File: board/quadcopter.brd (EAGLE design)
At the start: 100 x 80 mm, 41 parts, among them IC1 LD1117V33

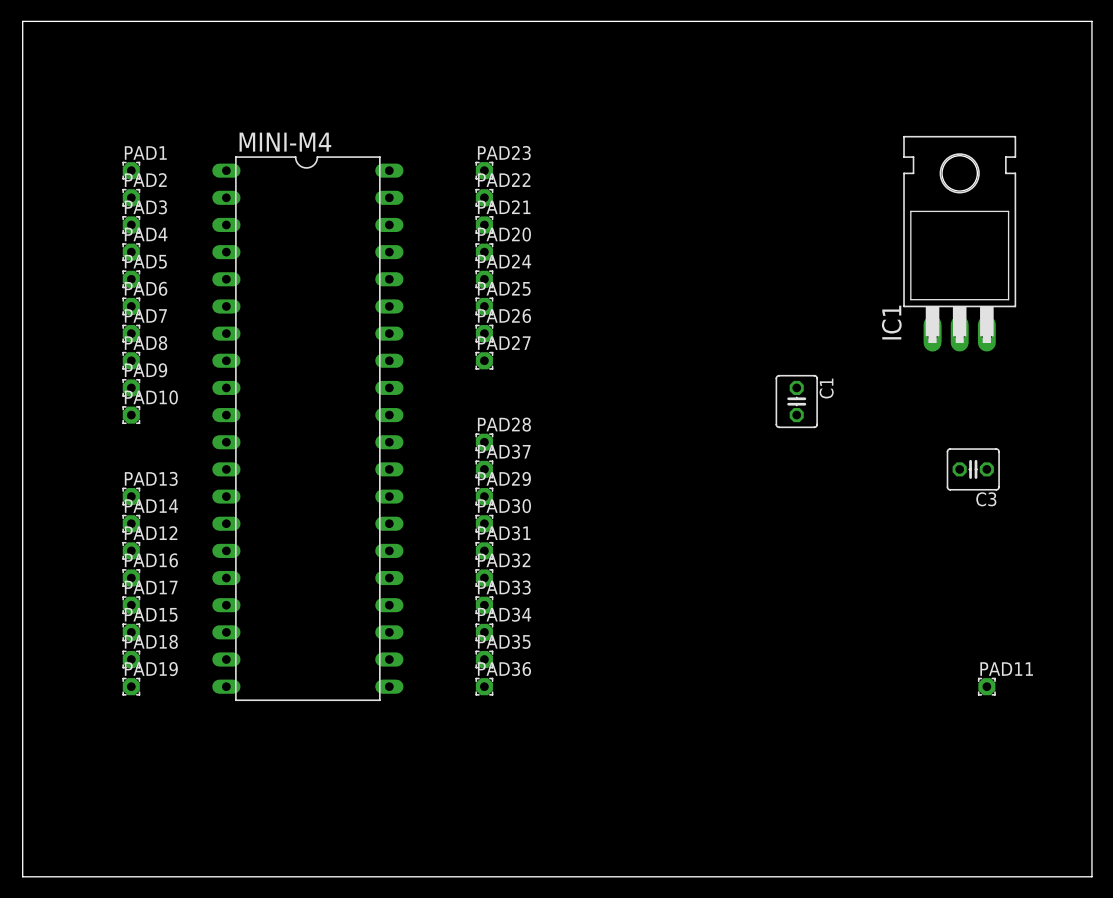
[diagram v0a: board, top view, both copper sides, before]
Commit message: updated the board layout and routed the voltage regulator
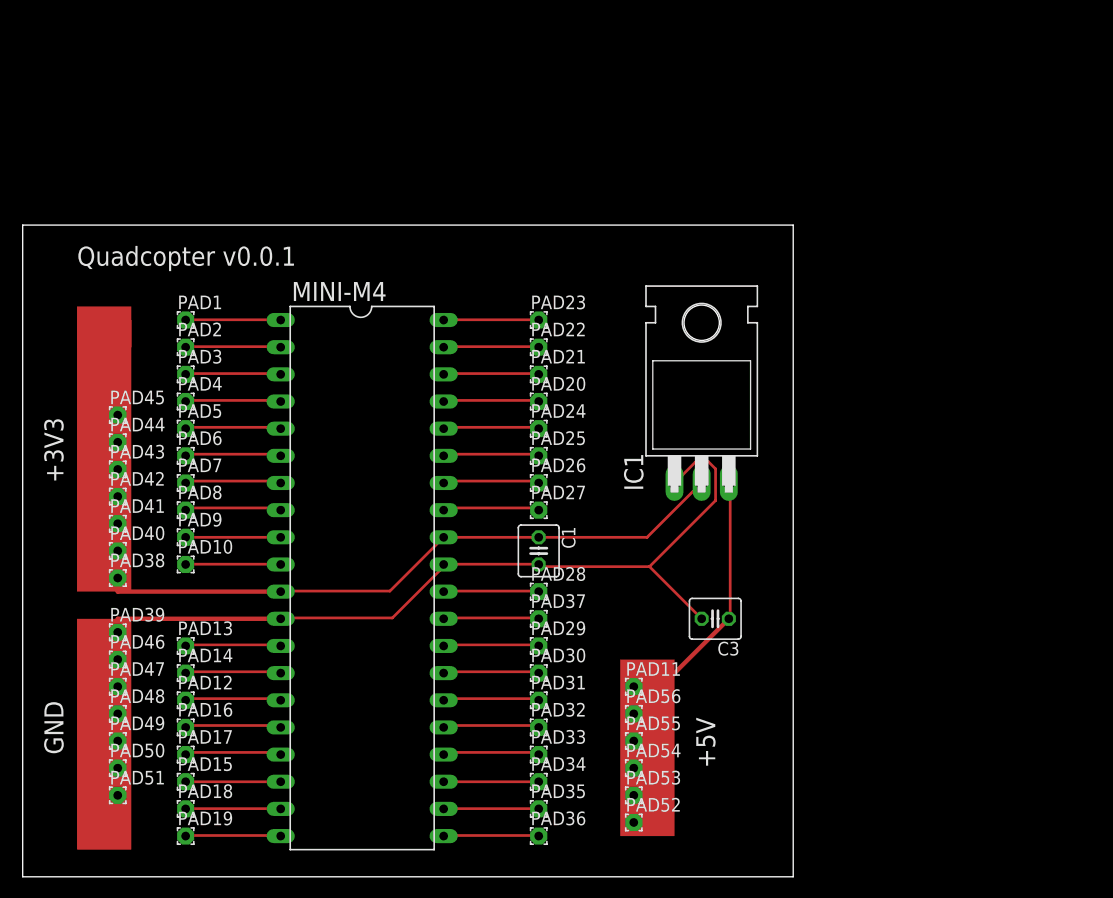
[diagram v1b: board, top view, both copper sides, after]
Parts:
- added PAD38, PAD39, PAD40, PAD41, PAD42, PAD43, PAD44, PAD45, PAD46, PAD47, PAD48, PAD49, PAD50, PAD51, PAD52, PAD53, PAD54, PAD55, PAD56: (no value), wirepad:1,6/0,8
- moved PAD11 33.0 mm to (57.1, 17.8)
- moved C1 27.9 mm to (48.3, 30.5)
- moved C3 27.9 mm to (64.8, 24.1)
- moved IC1 27.9 mm to (63.5, 47.0)
- moved PAD1 14.9 mm to (15.2, 52.1)
- moved PAD5 14.9 mm to (15.2, 41.9)
- moved PAD6 14.9 mm to (15.2, 39.4)
- moved PAD13 14.9 mm to (15.2, 21.6)
- moved PAD14 14.9 mm to (15.2, 19.1)
- moved PAD23 14.9 mm to (48.3, 52.1)
- moved PAD24 14.9 mm to (48.3, 41.9)
- moved PAD25 14.9 mm to (48.3, 39.4)
- moved PAD16 14.9 mm to (15.2, 14.0)
- moved PAD18 14.9 mm to (15.2, 6.35)
- moved PAD19 14.9 mm to (15.2, 3.81)
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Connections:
- net GND: now also PAD39.1, PAD46.1, PAD47.1, PAD48.1, PAD49.1, PAD50.1, PAD51.1
- net N$15: now also PAD52.1, PAD53.1, PAD54.1, PAD55.1, PAD56.1
- net VCC: now also PAD38.1, PAD40.1, PAD41.1, PAD42.1, PAD43.1, PAD44.1, PAD45.1
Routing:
- net GND: track 0.00 -> 76.9 mm
- net VCC: track 0.00 -> 60.1 mm
- net N$15: track 0.00 -> 24.4 mm
- net N$27: track 0.00 -> 9.18 mm
- net N$37: track 0.00 -> 9.18 mm
- net N$8: track 0.00 -> 9.14 mm
- net N$12: track 0.00 -> 9.14 mm
- net N$28: track 0.00 -> 9.13 mm
- net N$36: track 0.00 -> 9.13 mm
- net N$7: track 0.00 -> 9.10 mm
- net N$11: track 0.00 -> 9.10 mm
- net N$34: track 0.00 -> 9.09 mm
- net N$26: track 0.00 -> 9.09 mm
- net N$5: track 0.00 -> 9.06 mm
- net N$16: track 0.00 -> 9.06 mm
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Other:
- board size 100 x 80 mm -> 72.1 x 61 mm
- board text added: "+3V3"
- board text added: "+5V"
- board text added: "GND"
- board text added: "Quadcopter v0.0.1"

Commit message: the quadcopter board is shrunk to fit the frame
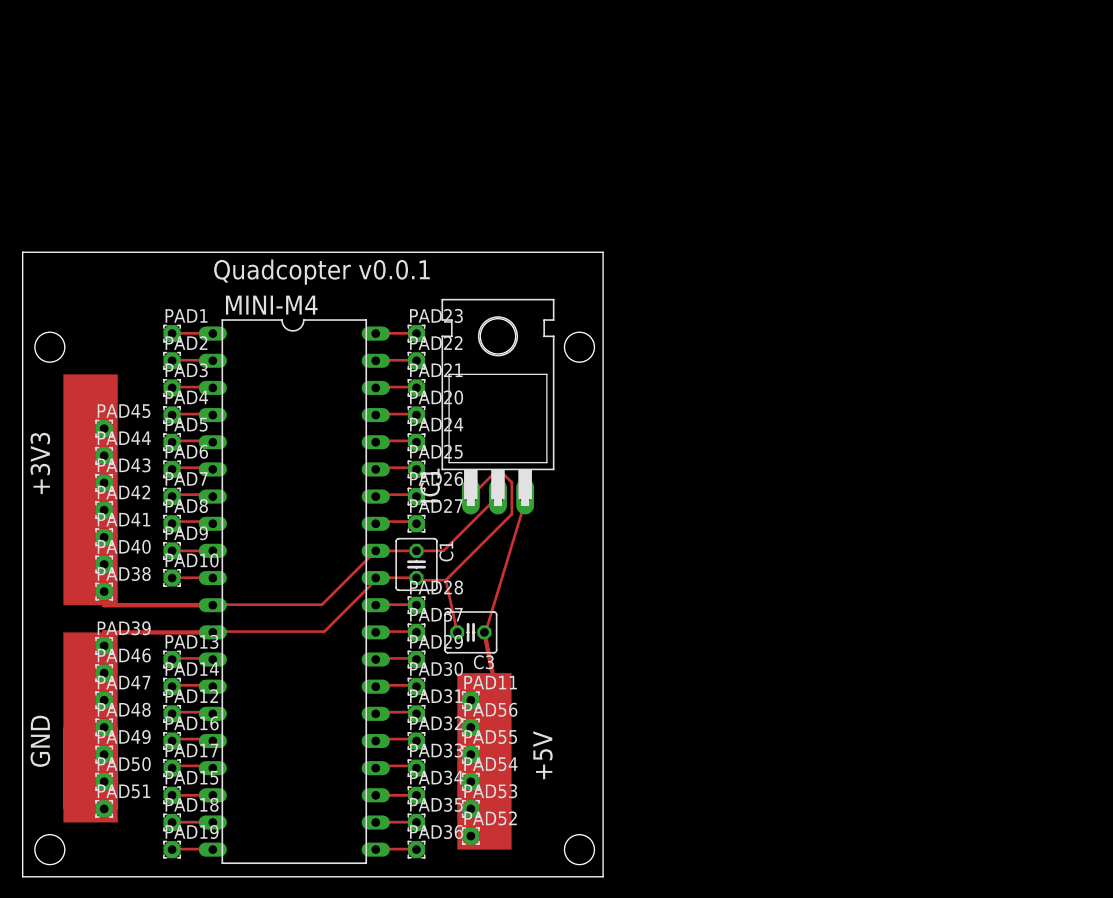
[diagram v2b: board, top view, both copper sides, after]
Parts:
- moved C3 22.9 mm to (41.9, 22.9)
- moved IC1 19.1 mm to (44.5, 45.7)
- moved PAD11 15.3 mm to (41.9, 16.5)
- moved PAD52 15.3 mm to (41.9, 3.81)
- moved PAD53 15.3 mm to (41.9, 6.35)
- moved PAD54 15.3 mm to (41.9, 8.89)
- moved PAD55 15.3 mm to (41.9, 11.4)
- moved PAD56 15.3 mm to (41.9, 14.0)
- moved C1 11.5 mm to (36.8, 29.2)
- moved PAD20 11.5 mm to (36.8, 43.2)
- moved PAD21 11.5 mm to (36.8, 45.7)
- moved PAD22 11.5 mm to (36.8, 48.3)
- moved PAD23 11.5 mm to (36.8, 50.8)
- moved PAD24 11.5 mm to (36.8, 40.6)
- moved PAD25 11.5 mm to (36.8, 38.1)
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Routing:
- net N$15: track 24.4 -> 32.6 mm
- net N$27: track 9.18 -> 4.10 mm
- net N$28: track 9.13 -> 4.05 mm
- net N$8: track 9.14 -> 4.06 mm
- net N$7: track 9.10 -> 4.02 mm
- net N$38: track 8.92 -> 3.84 mm
- net N$39: track 8.89 -> 3.81 mm
- net N$37: track 9.18 -> 4.10 mm
- net N$35: track 9.05 -> 3.97 mm
- net N$34: track 9.09 -> 4.01 mm
- net N$33: track 9.02 -> 3.94 mm
- net N$32: track 8.98 -> 3.90 mm
- net N$26: track 9.09 -> 4.01 mm
- net N$25: track 9.05 -> 3.97 mm
- net N$24: track 8.98 -> 3.90 mm
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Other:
- board size 72.1 x 61 mm -> 54.3 x 58.4 mm

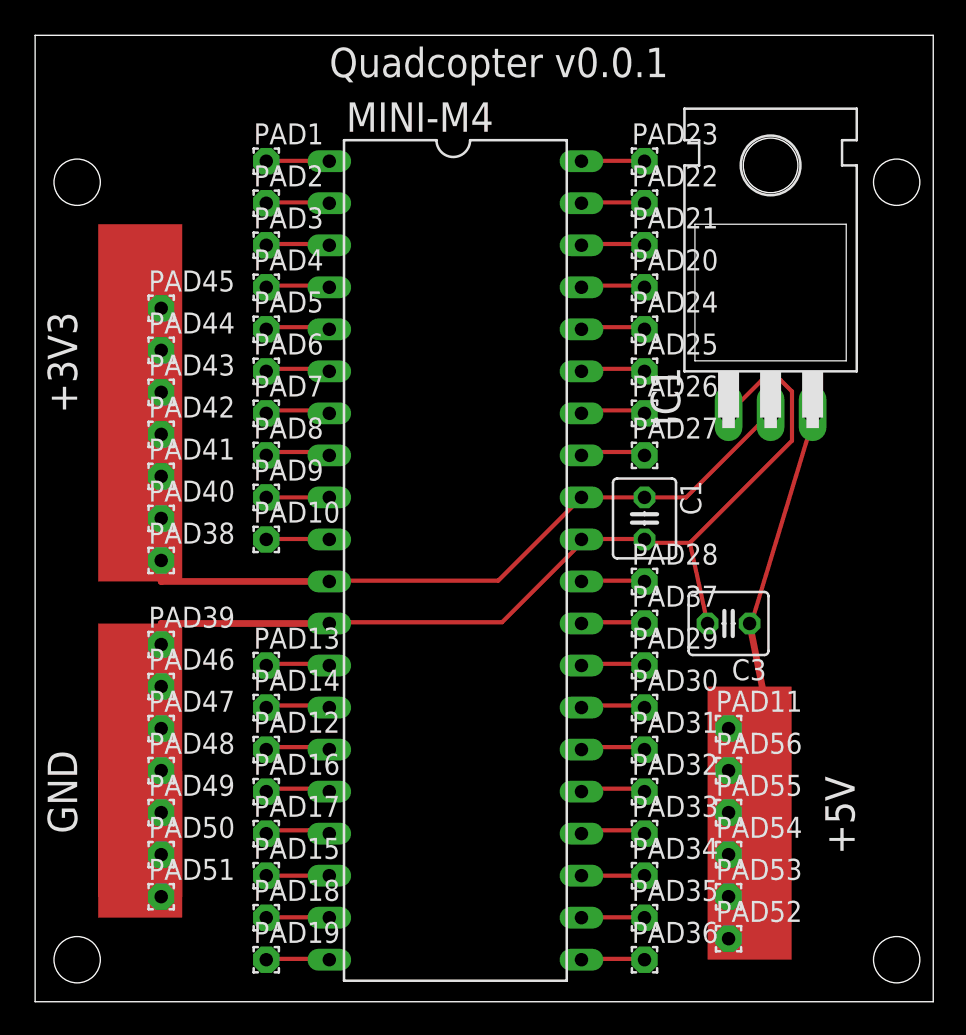
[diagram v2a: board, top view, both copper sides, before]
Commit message: updated quadcopter board to accomodate the 9dof
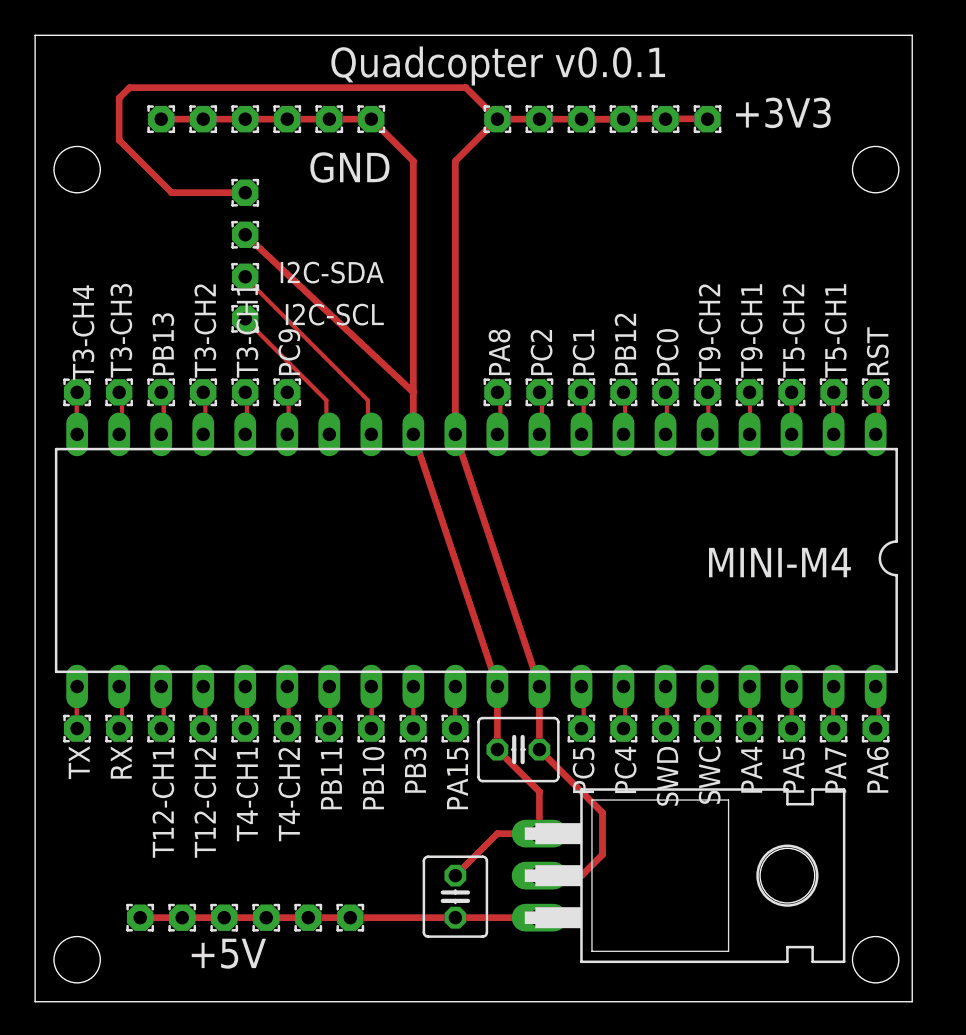
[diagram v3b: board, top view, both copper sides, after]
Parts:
- removed PAD1, PAD10, PAD12, PAD13, PAD14, PAD15, PAD16, PAD17, PAD18, PAD19, PAD2, PAD20, PAD21, PAD22, PAD23, PAD24, PAD25, PAD26, PAD27, PAD28, PAD29, PAD3, PAD30, PAD31, PAD32, PAD33, PAD34, PAD35, PAD36, PAD37, PAD4, PAD5, PAD6, PAD7, PAD8, PAD9: (no value), wirepad:1,6/0,8
- added I2C-SCL, I2C-SDA, PA15, PA4, PA5, PA6, PA7, PA8, PB10, PB11, PB12, PB13, PB3, PC0, PC1, PC2, PC4, PC5, PC9, RST, RX, SWC, SWD, T12-CH1, T12-CH2, T3-CH1, T3-CH2, T3-CH3, T3-CH4, T4-CH1, T4-CH2, T5-CH1, T5-CH2, T9-CH1, T9-CH2, TX: (no value), wirepad:1,6/0,8
- moved PAD51 47.0 mm to (7.62, 53.3), turned to 270 degrees
- moved PAD50 44.5 mm to (10.2, 53.3), turned to 270 degrees
- moved PAD49 42.2 mm to (12.7, 53.3), turned to 270 degrees
- moved PAD48 40.1 mm to (15.2, 53.3), turned to 270 degrees
- moved IC1 38.3 mm to (40.6, 7.62), turned to 270 degrees
- moved PAD47 38.2 mm to (17.8, 53.3), turned to 270 degrees
- moved PAD46 36.6 mm to (20.3, 53.3), turned to 270 degrees
- moved PAD52 35.6 mm to (6.35, 5.08)
- moved PAD38 35.1 mm to (30.5, 53.3), turned to 270 degrees
- moved PAD45 34.9 mm to (40.6, 53.3), turned to 270 degrees
- moved PAD44 33.5 mm to (38.1, 53.3), turned to 270 degrees
- moved PAD54 33.2 mm to (8.89, 5.08)
- moved PAD43 32.5 mm to (35.6, 53.3), turned to 270 degrees
- moved PAD42 31.8 mm to (33.0, 53.3), turned to 270 degrees
- moved PAD40 31.5 mm to (27.9, 53.3), turned to 270 degrees
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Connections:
- net N$1: now also T5-CH1.1; no longer PAD2.1
- net N$10: now also PA8.1; no longer PAD10.1
- net N$11: now also T3-CH1.1; no longer PAD16.1
- net N$12: now also T3-CH2.1; no longer PAD17.1
- net N$13: now also I2C-SDA.1; no longer PAD13.1
- net N$14: now also I2C-SCL.1; no longer PAD14.1
- net N$16: now also PC9.1; no longer PAD12.1
- net N$17: now also PA6.1; no longer PAD23.1
- net N$18: now also PB13.1; no longer PAD15.1
- net N$19: now also T3-CH3.1; no longer PAD18.1
- net N$2: now also RST.1; no longer PAD1.1
- net N$20: now also T3-CH4.1; no longer PAD19.1
- net N$21: now also PA7.1; no longer PAD22.1
- net N$23: now also PA4.1; no longer PAD20.1
- net N$24: now also PA5.1; no longer PAD21.1
- net N$25: now also SWC.1; no longer PAD24.1
- net N$26: now also SWD.1; no longer PAD25.1
- net N$27: now also PC5.1; no longer PAD27.1
- net N$28: now also PC4.1; no longer PAD26.1
- net N$3: now also T5-CH2.1; no longer PAD3.1
- net N$31: now also PA15.1; no longer PAD28.1
- net N$32: now also PB3.1; no longer PAD37.1
- net N$33: now also PB10.1; no longer PAD29.1
- net N$34: now also T4-CH2.1; no longer PAD31.1
- net N$35: now also PB11.1; no longer PAD30.1
- net N$36: now also T4-CH1.1; no longer PAD32.1
- net N$37: now also T12-CH2.1; no longer PAD33.1
- net N$38: now also RX.1; no longer PAD35.1
- net N$39: now also T12-CH1.1; no longer PAD34.1
- net N$4: now also T9-CH1.1; no longer PAD4.1
- net N$40: now also TX.1; no longer PAD36.1
- net N$5: now also PC0.1; no longer PAD6.1
- net N$6: now also T9-CH2.1; no longer PAD5.1
- net N$7: now also PB12.1; no longer PAD7.1
- net N$8: now also PC1.1; no longer PAD8.1
- net N$9: now also PC2.1; no longer PAD9.1
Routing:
- net VCC: track 57.5 -> 104.6 mm
- net N$13: track 3.90 -> 12.8 mm
- net N$15: track 32.6 -> 24.1 mm
- net GND: track 72.5 -> 80.6 mm
- net N$14: track 3.93 -> 9.19 mm
- net N$37: track 4.10 -> 2.65 mm
- net N$27: track 4.10 -> 2.65 mm
- net N$36: track 4.05 -> 2.62 mm
- net N$28: track 4.05 -> 2.62 mm
- net N$34: track 4.01 -> 2.59 mm
- net N$26: track 4.01 -> 2.59 mm
- net N$25: track 3.97 -> 2.56 mm
- net N$35: track 3.97 -> 2.56 mm
- net N$33: track 3.94 -> 2.55 mm
- net N$23: track 3.94 -> 2.55 mm
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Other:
- board size 54.3 x 58.4 mm -> 53 x 58.4 mm

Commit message: added the capacitor label to the board because I keep forgetting what it is
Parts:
- C1: value 10uF -> 10uF 106
- C3: value 100nF -> 100nF 104
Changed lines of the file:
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@@
 </autorouter>
 <elements>
-<element name="C1" library="rcl" package="C025-040X050" value="10uF" x="29.21" y="15.24" smashed="yes" rot="R180">
+<element name="C1" library="rcl" package="C025-040X050" value="10uF 106" x="29.21" y="15.24" smashed="yes" rot="R180">
 <attribute name="VALUE" x="31.496" y="13.589" size="1.27" layer="27" ratio="10" rot="R180"/>
 </element>
-<element name="C3" library="rcl" package="C025-040X050" value="100nF" x="25.4" y="6.35" smashed="yes" rot="R90">
+<element name="C3" library="rcl" package="C025-040X050" value="100nF 104" x="25.4" y="6.35" smashed="yes" rot="R90">
 <attribute name="VALUE" x="28.829" y="4.064" size="1.27" layer="27" ratio="10" rot="R90"/>
 </element>
